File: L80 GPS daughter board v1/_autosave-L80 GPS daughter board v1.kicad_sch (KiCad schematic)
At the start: 14 parts, among them J1 Conn_01x06_Socket, J2 THD2528-11SD-GF, SW1 SW_Push, U1 AP2112K-3.3, U2 L80-R, U3 MCP73831-2-OT

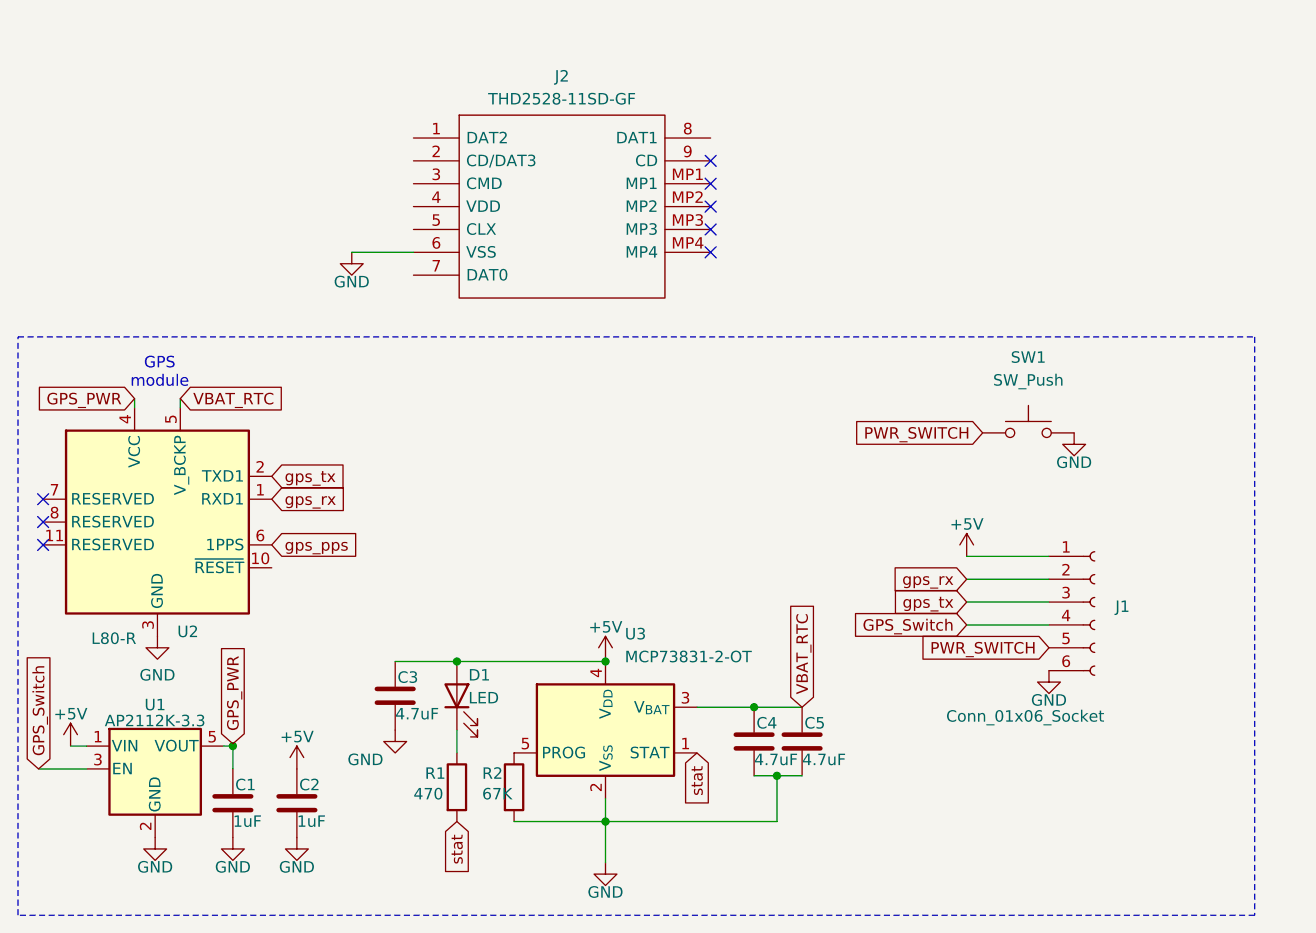
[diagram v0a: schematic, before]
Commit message: modefied gps board to handle sdcard operations and power input
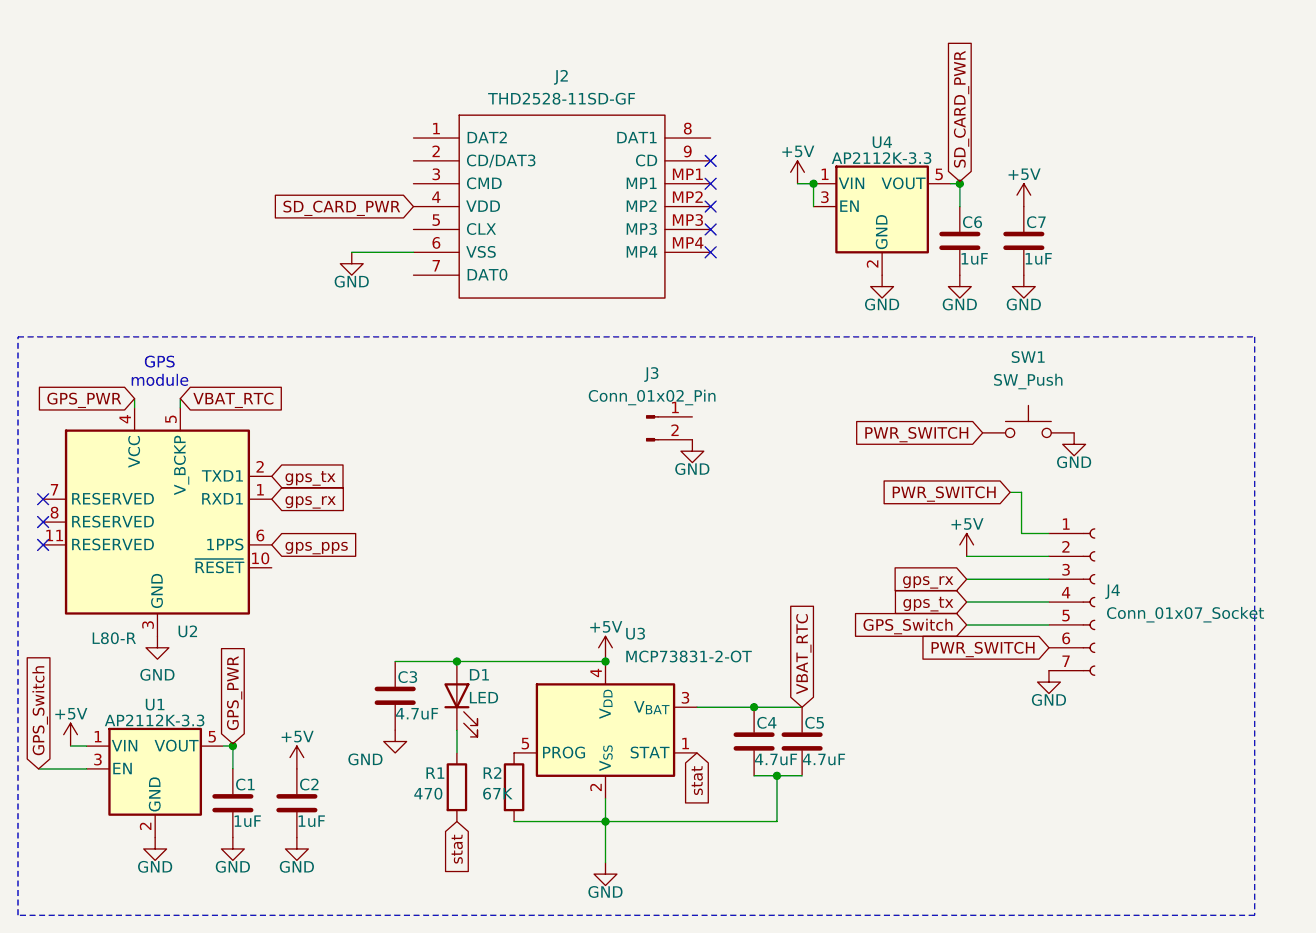
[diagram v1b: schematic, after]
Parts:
- removed J1: Conn_01x06_Socket, Connector_PinHeader_2.54mm:PinHeader_1x06_P2.54mm_Vertical, symbol Connector:Conn_01x06_Socket
- added C6, C7: 1uF, Capacitor_SMD:C_0603_1608Metric, symbol Device:C
- added J3: Conn_01x02_Pin, Connector_PinHeader_2.54mm:PinHeader_1x02_P2.54mm_Vertical, symbol Connector:Conn_01x02_Pin
- added J4: Conn_01x07_Socket, Connector_PinSocket_2.54mm:PinSocket_1x07_P2.54mm_Vertical, symbol Connector:Conn_01x07_Socket
- added U4: AP2112K-3.3, Package_TO_SOT_SMD:SOT-23-5, symbol Regulator_Linear:AP2112K-3.3
- J2: footprint THD252811SDGF -> KiCad:THD252811SDGF
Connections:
- net +5V: now also C7.1, J4.2 (Pin_2), U4.1 (VIN), U4.3 (EN)
- net GND: now also C6.2, C7.2, J3.2 (Pin_2), J4.7 (Pin_7), U4.2 (GND)
- net GPS_Switch: now also J4.5 (Pin_5)
- net PWR_SWITCH: now also J4.1 (Pin_1), J4.6 (Pin_6)
- net gps_rx: now also J4.3 (Pin_3)
- net gps_tx: now also J4.4 (Pin_4)
- net SD_CARD_PWR: now reaches J2.4 (VDD)
- net SD_CARD_PWR: now also C6.1, U4.5 (VOUT)
